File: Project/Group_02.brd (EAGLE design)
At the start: 71.1 x 40.6 mm, 29 parts, among them J1 POWER_JACKPTH_LOCK, U1 +12v

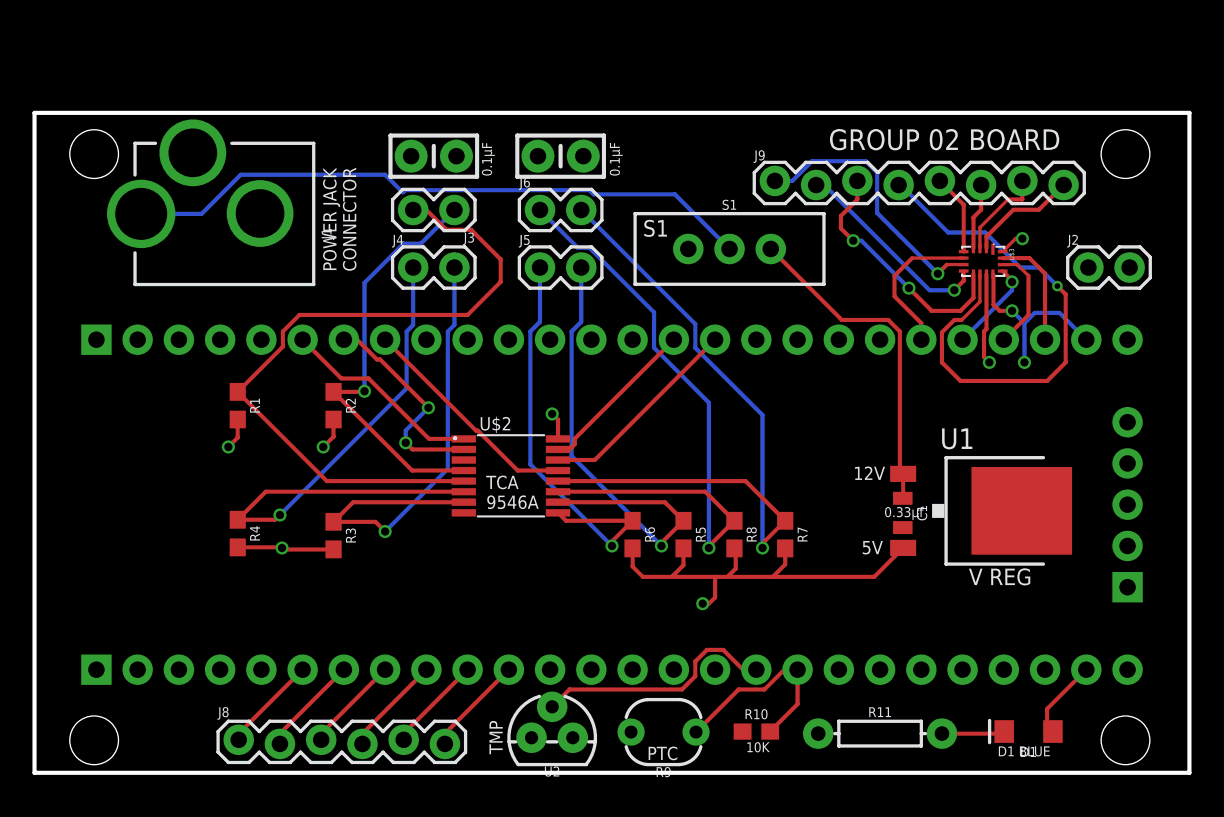
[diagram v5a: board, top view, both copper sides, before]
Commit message: Aggiustamento posizionamento pin
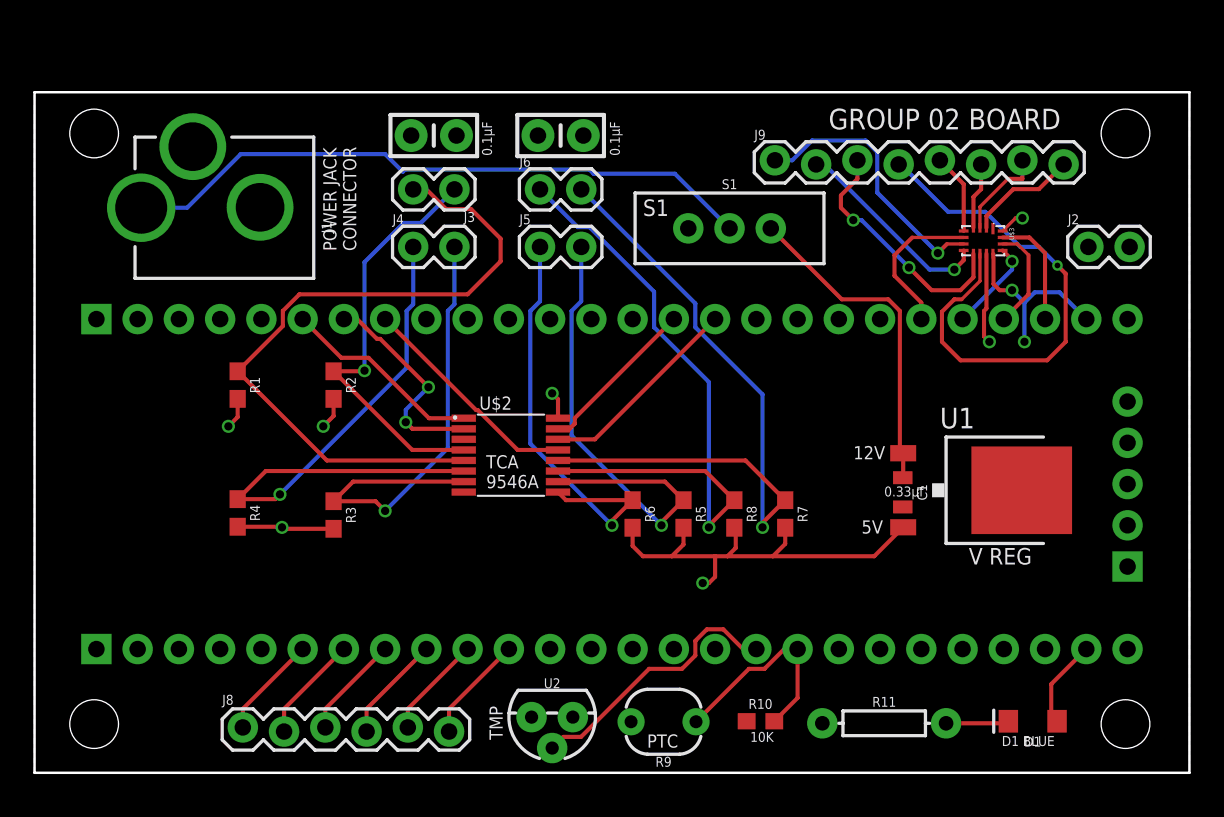
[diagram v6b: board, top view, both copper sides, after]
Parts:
- moved C2 1.27 mm to (24.6, 39.2)
- moved C3 1.27 mm to (32.4, 39.2)
- moved J3 1.27 mm to (25.9, 35.9)
- moved J6 1.27 mm to (31.1, 35.9)
- moved U2 1.27 mm to (31.9, 3.43), turned to 180 degrees
- moved C1 1.27 mm to (53.5, 17.3)
- moved J2 1.27 mm to (64.9, 32.4)
- moved J4 1.27 mm to (23.3, 32.4)
- moved J5 1.27 mm to (31.1, 32.4)
- moved R1 1.27 mm to (12.5, 23.9)
- moved R2 1.27 mm to (18.4, 23.9)
- moved R3 1.27 mm to (18.4, 15.9)
- moved R4 1.27 mm to (12.5, 16.0)
- moved R5 1.27 mm to (40.0, 15.9)
- moved R6 1.27 mm to (36.8, 15.9)
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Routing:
- net TEMP_OUT: track 15.1 -> 16.6 mm
- net PHOTO_OUT: track 12.4 -> 13.1 mm
- net N$8: track 4.96 -> 5.49 mm
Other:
- board size 71.1 x 40.6 mm -> 71.1 x 41.9 mm

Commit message: File completi
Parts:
- moved C3 44.0 mm to (8.88, 2.03), turned to 180 degrees
- moved C2 38.9 mm to (35.9, 2.03)
- moved U2 34.7 mm to (34.9, 38.0)
- moved R9 34.1 mm to (40.6, 37.2), turned to 90 degrees
- moved J8 2.50 mm to (15.2, 2.16)
- moved J6 2.40 mm to (29.1, 34.7)
- moved J5 2.40 mm to (29.1, 31.1)
- moved S1 2.33 mm to (41.9, 31.4)
- moved J1 1.80 mm to (19.2, 33.5)
- moved J2 1.80 mm to (63.6, 31.1)
- moved J3 1.80 mm to (24.6, 34.7)
- moved R5 1.80 mm to (38.7, 14.7)
- moved R7 1.80 mm to (45.0, 14.7)
- moved R8 1.80 mm to (41.8, 14.7)
- moved U$3 1.80 mm to (57.1, 31.5)
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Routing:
- net PHOTO_OUT: track 13.1 -> 38.0 mm
- net TEMP_OUT: track 16.6 -> 36.8 mm
- net N$14: track 32.5 -> 14.9 mm
- net GND: track 11.4 -> 6.94 mm, vias 2 -> 1
- net N$17: track 16.7 -> 13.8 mm
- net 5V: track 45.8 -> 43.1 mm
- net N$16: track 12.6 -> 15.2 mm, vias 1 -> 0
- net N$6: track 6.35 -> 4.19 mm
- net N$2: track 6.35 -> 4.19 mm
- net N$7: track 6.61 -> 4.44 mm
- net N$5: track 6.61 -> 4.44 mm
- net N$4: track 6.35 -> 4.19 mm
- net N$3: track 6.61 -> 4.44 mm
- net MUX_OUT: track 9.33 -> 8.24 mm, vias 0 -> 1
- net 12V: track 20.4 -> 19.7 mm
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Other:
- board size 71.1 x 41.9 mm -> 68.6 x 40.6 mm

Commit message: Aggiunta isolamento
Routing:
- net GND: track 6.94 -> 11.9 mm
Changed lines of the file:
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@@
 <setting verticaltext="up"/>
 </settings>
-<grid distance="0.05" unitdist="inch" unit="mm" style="lines" multiple="1" display="yes" altdistance="0.005" altunitdist="inch" altunit="mil"/>
+<grid distance="0.05" unitdist="inch" unit="mil" style="lines" multiple="1" display="yes" altdistance="0.005" altunitdist="inch" altunit="mil"/>
 <layers>
 <layer number="1" name="Top" color="4" fill="1" visible="yes" active="yes"/>
@@
 <contactref element="U$3" pad="12"/>
 <contactref element="C3" pad="2"/>
-<polygon width="0.254" layer="1">
+<polygon width="0.254" layer="1" isolate="0.3048">
 <vertex x="0" y="0"/>
 <vertex x="0" y="40.64"/>
@@
 <wire x1="58.293" y1="29.845" x2="62.357" y2="29.845" width="0.254" layer="16"/>
 <wire x1="62.357" y1="29.845" x2="63.627" y2="31.115" width="0.254" layer="16"/>
+<wire x1="26.02614375" y1="16.1586" x2="26.1964" y2="16.32885625" width="0.254" layer="1"/>
+<wire x1="26.1964" y1="18.94714375" x2="26.02614375" y2="19.1174" width="0.254" layer="1"/>
+<wire x1="26.1964" y1="16.32885625" x2="26.1964" y2="18.94714375" width="0.254" layer="1"/>
+<wire x1="25.167" y1="16.013" x2="25.3126" y2="16.1586" width="0.254" layer="1"/>
+<wire x1="25.3126" y1="16.1586" x2="26.02614375" y2="16.1586" width="0.254" layer="1"/>
+<wire x1="26.02614375" y1="19.1174" x2="25.3126" y2="19.1174" width="0.254" layer="1"/>
+<wire x1="25.3126" y1="19.1174" x2="25.167" y2="19.263" width="0.254" layer="1"/>
 </signal>
 <signal name="12V">
